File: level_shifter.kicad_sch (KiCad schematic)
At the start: 3 parts

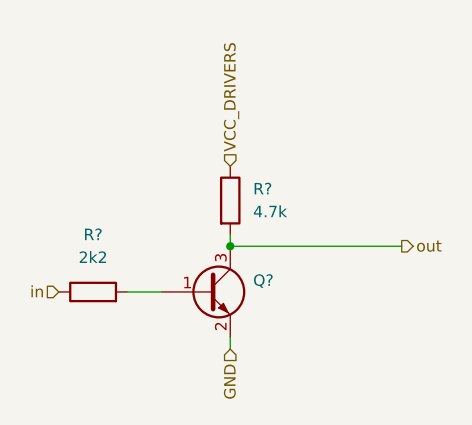
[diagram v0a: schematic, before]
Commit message: Refactored top sheet
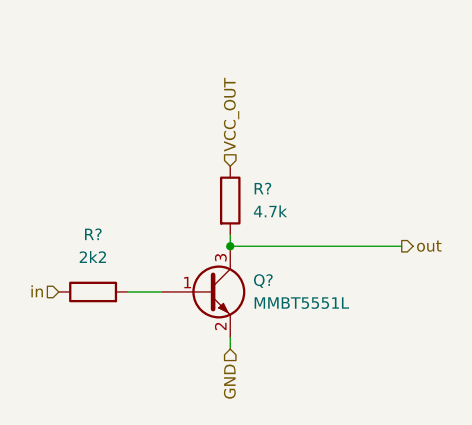
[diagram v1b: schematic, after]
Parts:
- Q?: value (none) -> MMBT5551L; footprint (none) -> Package_TO_SOT_SMD:SOT-23
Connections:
- net VCC_DRIVERS renamed VCC_OUT
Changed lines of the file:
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@@
     (effects (font (size 1.27 1.27)) (justify left))
   )
-  (hierarchical_label "VCC_DRIVERS" (shape input) (at 110.49 67.31 90)
+  (hierarchical_label "VCC_OUT" (shape input) (at 110.49 67.31 90)
     (effects (font (size 1.27 1.27)) (justify left))
   )
@@
       (effects (font (size 1.27 1.27)) (justify left))
     )
-    (property "Value" "" (id 1) (at 113.03 82.5499 0)
+    (property "Value" "MMBT5551L" (id 1) (at 113.03 82.5499 0)
       (effects (font (size 1.27 1.27)) (justify left))
     )
-    (property "Footprint" "" (id 2) (at 113.03 83.185 0)
+    (property "Footprint" "Package_TO_SOT_SMD:SOT-23" (id 2) (at 113.03 83.185 0)
       (effects (font (size 1.27 1.27) italic) (justify left) hide)
     )
